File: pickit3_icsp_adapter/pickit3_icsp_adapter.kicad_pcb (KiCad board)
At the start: 2 copper layers, 31.8 x 16.5 mm, 3 parts, among them J1 Conn_01x06_Male, J2 Conn_01x06

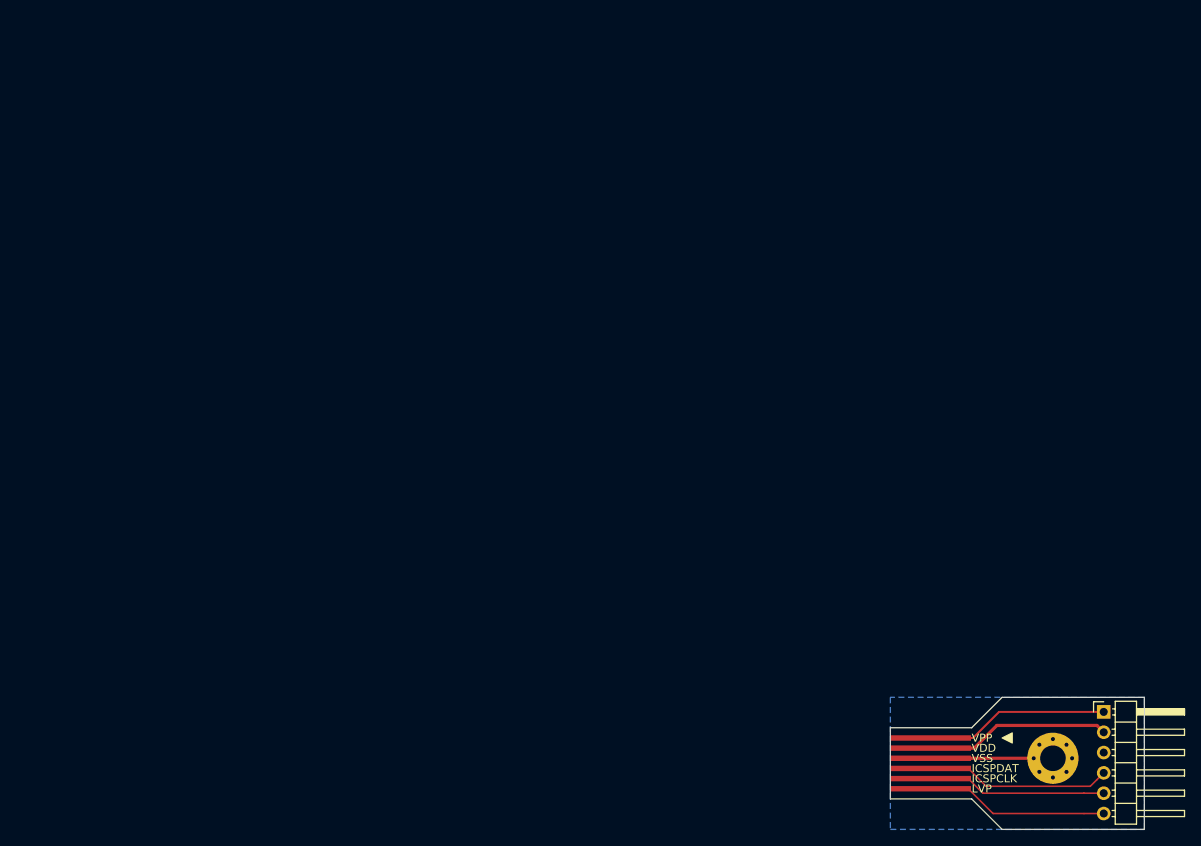
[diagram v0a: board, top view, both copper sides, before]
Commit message: ICSP Adapter v2.0
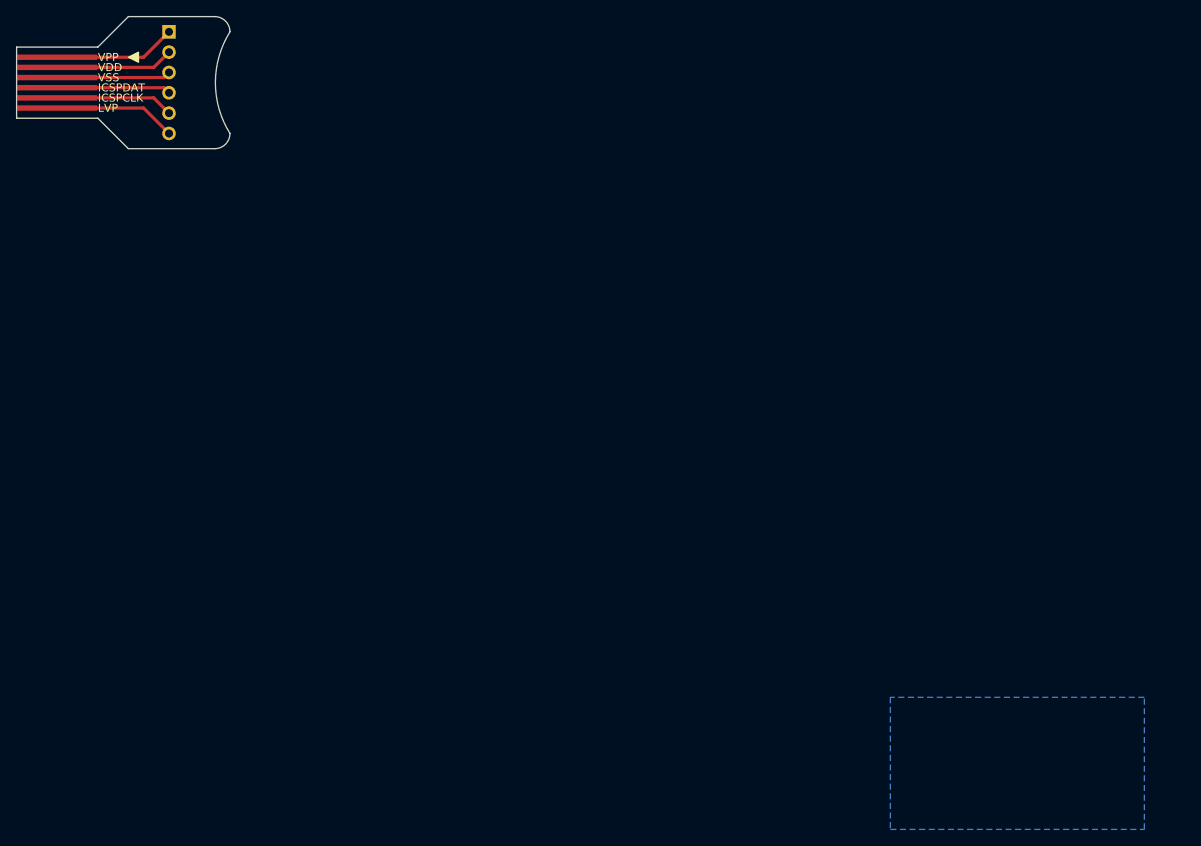
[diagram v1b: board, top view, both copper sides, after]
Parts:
- removed H1: MountingHole_Pad, MountingHole:MountingHole_3.2mm_M3_Pad_Via
- J1: footprint Connector_PinHeader_2.54mm:PinHeader_1x06_P2.54mm_Horizontal -> Connector_PinHeader_2.54mm:PinHeader_1x06_P2.54mm_Vertical; moved to B.Cu
- moved J1 144.5 mm to (19.1, 1.91), turned to 180 degrees
- moved J2 138.5 mm to (5.08, 8.89)
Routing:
- net /ICSPDAT: track 23.2 -> 14.2 mm
- net /VDD: track 23.1 -> 14.8 mm
- net /VPP: track 22.9 -> 15.3 mm
- net /LVP: track 22.9 -> 15.3 mm
- net /ICSPCLK: track 22.3 -> 14.8 mm
- net /VSS: track 15.2 -> 14.2 mm
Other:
- board size 31.8 x 16.5 mm -> 26.7 x 16.5 mm
- board text added: "Pickit3 POGO ICSP Adapter v1.1"
- board text removed: "Pickit3 POGO ICSP Adapter v1.0"

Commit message: Revise 2.0
* update silkscreen
* update README
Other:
- board text added: "Pickit3 POGO ICSP Adapter v2.0"
- board text removed: "Pickit3 POGO ICSP Adapter v1.1"
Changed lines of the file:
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@@
   )
   (setup
-    (last_trace_width 0.4)
+    (last_trace_width 0.25)
     (user_trace_width 0.2)
     (user_trace_width 0.25)
@@
     (descr "Through hole straight pin header, 1x06, 2.54mm pitch, single row")
     (tags "Through hole pin header THT 1x06 2.54mm single row")
-    (fp_text reference J1 (at 0 2.33 180) (layer B.SilkS)
+    (fp_text reference J1 (at 0 2.33 180) (layer B.SilkS) hide
       (effects (font (size 1 1) (thickness 0.15)) (justify mirror))
     )
@@
     (effects (font (size 1 1) (thickness 0.15)) (justify right mirror))
   )
-  (gr_text "Pickit3 POGO\nICSP Adapter v1.1" (at 1.27 6.35) (layer B.SilkS)
+  (gr_text "Pickit3 POGO\nICSP Adapter v2.0" (at 1.27 6.35) (layer B.SilkS)
     (effects (font (size 1 1) (thickness 0.15)) (justify right mirror))
   )

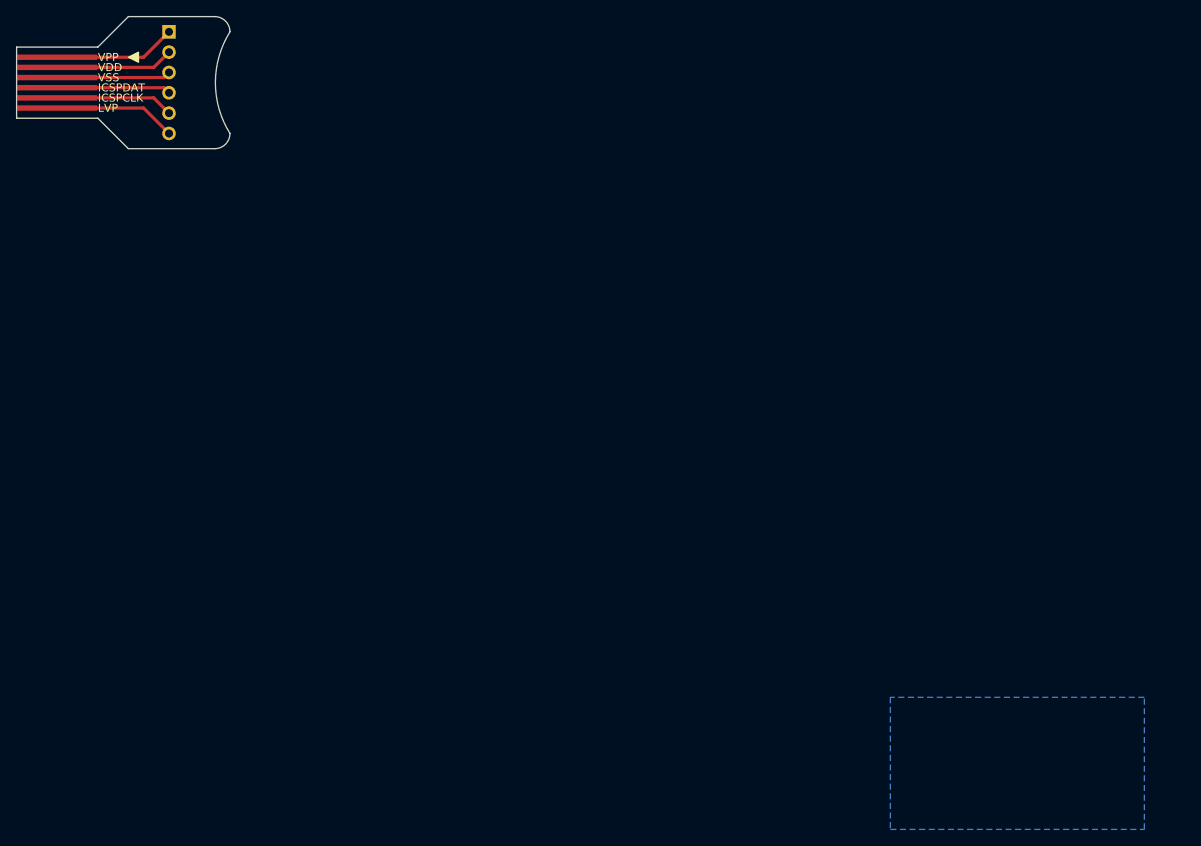
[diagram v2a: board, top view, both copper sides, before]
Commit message: Add footprint for ICSP pads
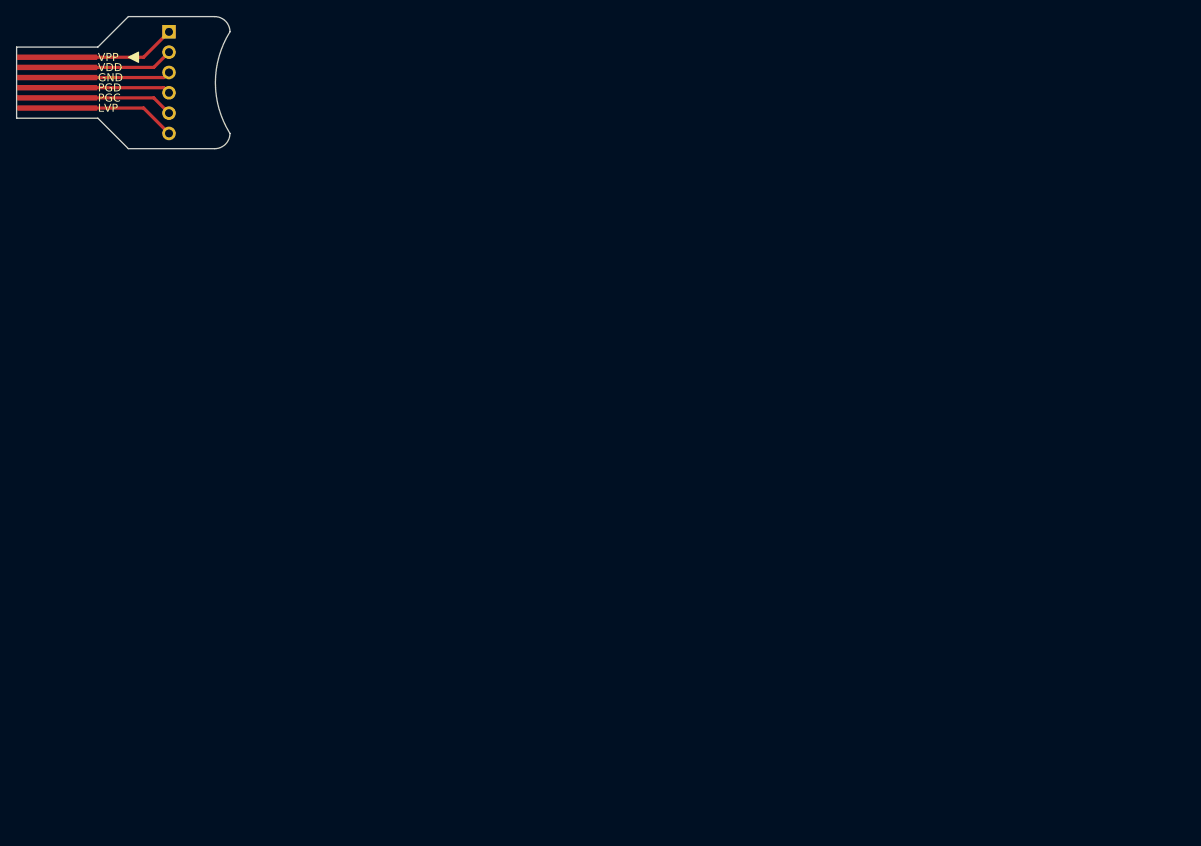
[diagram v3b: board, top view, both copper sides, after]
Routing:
- removed copper zone on B.Cu, net /VSS
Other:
- board text added: "GND"
- board text added: "PGC"
- board text added: "PGD"
- board text added: "pantsforbirds.com"
- board text removed: "ICSPCLK"
- board text removed: "ICSPDAT"
- board text removed: "VSS"
- board text removed: "johnmcnelly.com"
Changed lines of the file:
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@@
   (layers
     (0 F.Cu signal)
-    (31 B.Cu signal hide)
+    (31 B.Cu signal)
     (32 B.Adhes user)
     (33 F.Adhes user)
@@
     (descr "Through hole straight pin header, 1x06, 2.54mm pitch, single row")
     (tags "Through hole pin header THT 1x06 2.54mm single row")
-    (fp_text reference J1 (at 0 2.33 180) (layer B.SilkS) hide
+    (fp_text reference J1 (at -3.175 0 180) (layer B.SilkS) hide
       (effects (font (size 1 1) (thickness 0.15)) (justify mirror))
     )
@@
   (gr_line (start 10.16 12.7) (end 13.97 16.51) (layer Edge.Cuts) (width 0.15))
   (gr_poly (pts (xy 13.97 5.08) (xy 15.24 4.445) (xy 15.24 5.715)) (layer F.SilkS) (width 0.15))
-  (gr_text johnmcnelly.com (at 1.27 10.16) (layer B.SilkS)
+  (gr_text pantsforbirds.com (at 1.27 10.16) (layer B.SilkS)
     (effects (font (size 1 1) (thickness 0.15)) (justify right mirror))
   )
@@
     (effects (font (size 1 1) (thickness 0.15)) (justify left))
   )
-  (gr_text ICSPCLK (at 10.16 10.16) (layer F.SilkS)
-    (effects (font (size 1 1) (thickness 0.15)) (justify left))
-  )
-  (gr_text ICSPDAT (at 10.16 8.89) (layer F.SilkS)
-    (effects (font (size 1 1) (thickness 0.15)) (justify left))
-  )
-  (gr_text VSS (at 10.16 7.62) (layer F.SilkS)
+  (gr_text PGC (at 10.16 10.16) (layer F.SilkS)
+    (effects (font (size 1 1) (thickness 0.15)) (justify left))
+  )
+  (gr_text PGD (at 10.16 8.89) (layer F.SilkS)
+    (effects (font (size 1 1) (thickness 0.15)) (justify left))
+  )
+  (gr_text GND (at 10.16 7.62) (layer F.SilkS)
     (effects (font (size 1 1) (thickness 0.15)) (justify left))
   )
@@
   (segment (start 15.875 11.43) (end 19.05 14.605) (width 0.4) (layer F.Cu) (net 6))
   (segment (start 5.08 11.43) (end 15.875 11.43) (width 0.4) (layer F.Cu) (net 6))
-  (zone (net 1) (net_name /VSS) (layer B.Cu) (hatch edge 0.508)
-    (connect_pads (clearance 0.508))
-    (min_thickness 0.254)
-    (fill yes (arc_segments 16) (thermal_gap 0.508) (thermal_bridge_width 0.508))
-    (polygon
-      (pts
-        (xy 109.22 85.09) (xy 109.22 101.6) (xy 140.97 101.6) (xy 140.97 85.09)
-      )
-    )
-  )
 )
